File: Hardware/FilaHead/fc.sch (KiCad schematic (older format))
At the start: 7 parts, among them J0 Conn_2, J1 Conn_01x15_Female, J2 Conn_01x15_Female, J3 Conn_2

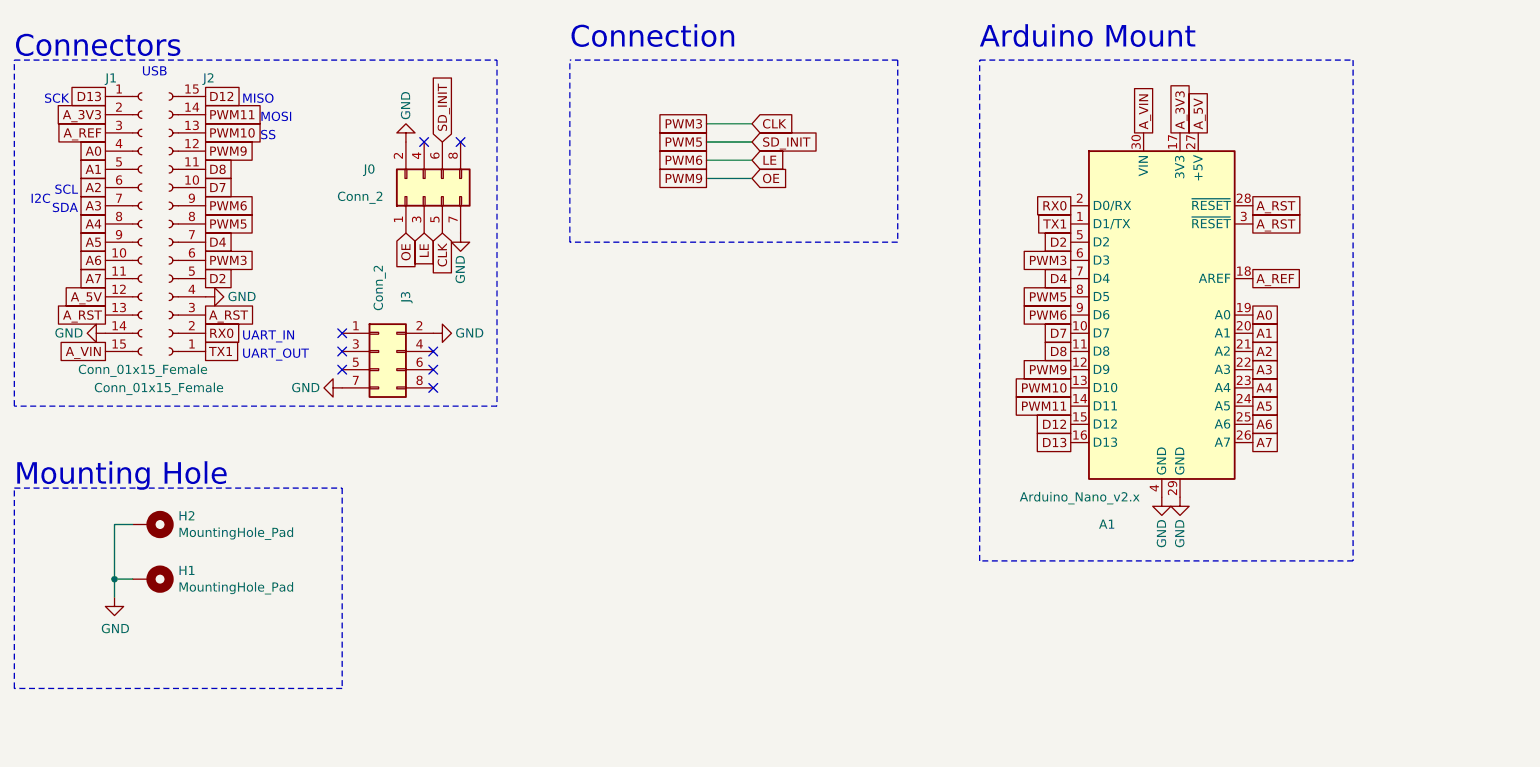
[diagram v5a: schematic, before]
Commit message: updated FilaHead v0.3
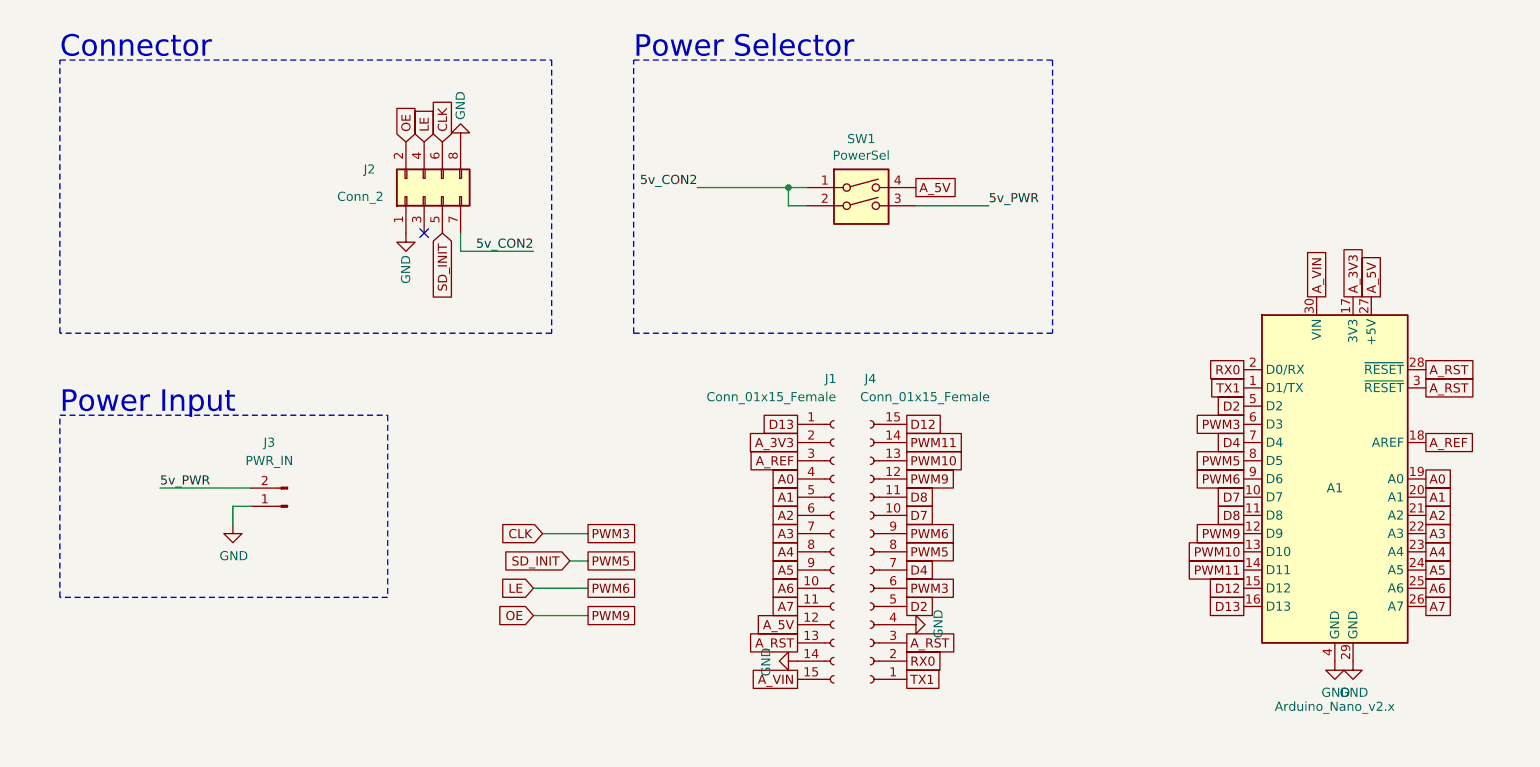
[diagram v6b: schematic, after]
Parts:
- removed H1, H2: MountingHole_Pad, MountingHole:MountingHole_3.2mm_M3_Pad_Via, symbol Mechanical:MountingHole_Pad
- removed J2: Conn_01x15_Female, Connector_PinHeader_2.54mm:PinHeader_1x15_P2.54mm_Vertical, symbol Connector:Conn_01x15_Female
- removed J3: Conn_2, Connector_PinHeader_2.54mm:PinHeader_2x04_P2.54mm_Vertical, symbol Connector_Generic:Conn_02x04_Odd_Even
- added J3: PWR_IN, Connector_PinHeader_2.54mm:PinHeader_1x02_P2.54mm_Horizontal, symbol Connector:Conn_01x02_Male
- added J4: Conn_01x15_Female, Connector_PinHeader_2.54mm:PinHeader_1x15_P2.54mm_Vertical, symbol Connector:Conn_01x15_Female
- added SW1: PowerSel, Button_Switch_SMD:SW_DIP_SPSTx02_Slide_KingTek_DSHP02TS_W7.62mm_P1.27mm, symbol Switch:SW_DIP_x02
- J2: renamed from J0; footprint Connector_PinHeader_2.54mm:PinHeader_2x04_P2.54mm_Vertical -> Connector_PinSocket_2.54mm:PinSocket_2x04_P2.54mm_Vertical
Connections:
- net A_5V: now also SW1.4
- net A_RST: now also J4.3 (Pin_3)
- net CLK: now also J2.6 (Pin_6), J4.6 (Pin_6); no longer J2.5 (Pin_5)
- net D12: now also J4.15 (Pin_15)
- net D2: now also J4.5 (Pin_5)
- net D4: now also J4.7 (Pin_7)
- net D7: now also J4.10 (Pin_10)
- net D8: now also J4.11 (Pin_11)
- net GND: now also J2.1 (Pin_1), J2.8 (Pin_8), J3.1 (Pin_1), J4.4 (Pin_4); no longer J2.2 (Pin_2), J2.7 (Pin_7)
- net LE: now also J2.4 (Pin_4), J4.9 (Pin_9); no longer J2.3 (Pin_3)
- net OE: now also J2.2 (Pin_2), J4.12 (Pin_12); no longer J2.1 (Pin_1)
- net PWM10: now also J4.13 (Pin_13)
- net PWM11: now also J4.14 (Pin_14)
- net PWM5: now also J2.5 (Pin_5), J4.8 (Pin_8); no longer J2.6 (Pin_6)
- net RX0: now also J4.2 (Pin_2)
- net TX1: now also J4.1 (Pin_1)
- new net 5v_CON2: J2.7 (Pin_7), SW1.1, SW1.2
- new net 5v_PWR: J3.2 (Pin_2), SW1.3
- no-connect marks 8 -> 1
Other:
- note added: "Connector"
- note added: "Power Input"
- note added: "Power Selector"
- note removed: "Arduino Mount"
- note removed: "Connection"
- note removed: "Connectors"
- note removed: "I2C"
- note removed: "MISO"
- note removed: "MOSI"
- note removed: "Mounting Hole"
- note removed: "SCK"
- note removed: "SCL"
- note removed: "SDA"
- note removed: "SS"
- note removed: "UART_IN"
- note removed: "UART_OUT"
- note removed: "USB"
